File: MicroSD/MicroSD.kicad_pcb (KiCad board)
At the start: 2 copper layers, 25.4 x 26.7 mm, 18 parts, among them J1 Conn_01x04, J2 Conn_01x04, U1 AP7365, U2 4050

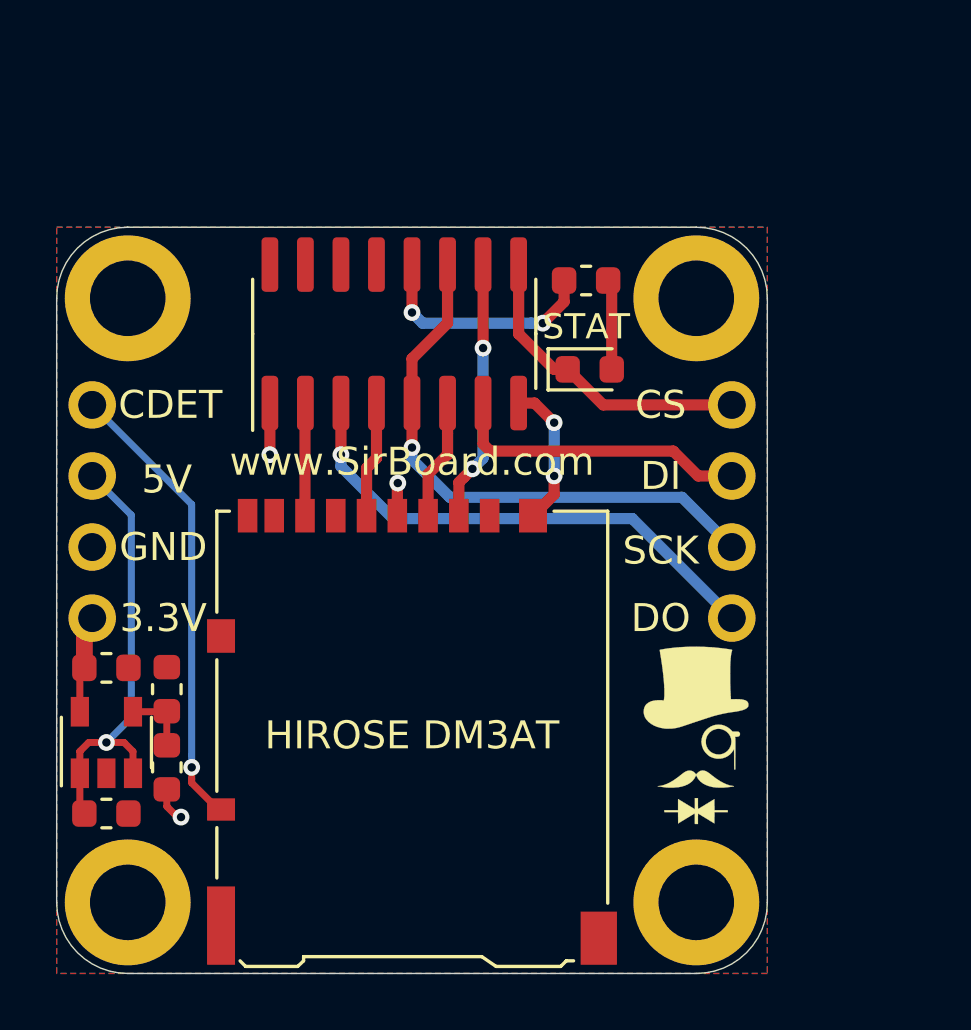
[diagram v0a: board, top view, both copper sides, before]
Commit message: MicroSDv2 Removed and MicroSD and MicroSD_DualVoltage Updated
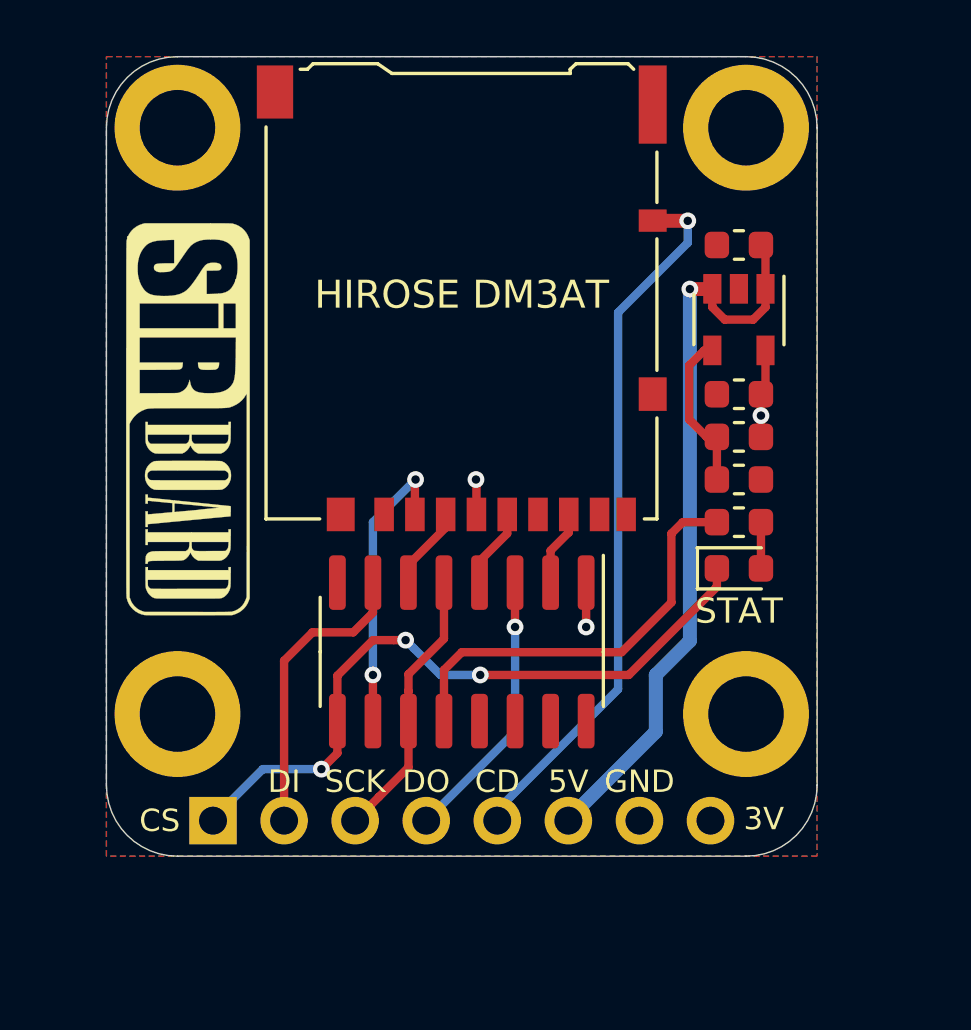
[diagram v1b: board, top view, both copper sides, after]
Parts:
- removed the G*** at (72.8, 43.1)
- removed J2: Conn_01x04, Connector_PinHeader_2.54mm:PinHeader_1x04_P2.54mm_Vertical
- added G***: LOGO, logo:SirBoard140x44, F.Cu at (54.6, 31.8)
- J1: value Conn_01x04 -> Conn_01x08; footprint Connector_PinHeader_2.54mm:PinHeader_1x04_P2.54mm_Vertical -> Connector_PinHeader_2.54mm:PinHeader_1x08_P2.54mm_Vertical; moved to B.Cu
- moved H3 35.4 mm to (74.5, 21.3), turned to 180 degrees
- moved H1 33.3 mm to (54.2, 21.3), turned to 180 degrees
- moved C1 30.4 mm to (74.3, 25.5), turned to 180 degrees
- moved U1 27.2 mm to (74.3, 28.2), turned to 270 degrees
- moved H4 26.6 mm to (74.5, 42.3), turned to 180 degrees
- moved C2 24.6 mm to (74.3, 30.9), turned to 180 degrees
- moved H2 23.8 mm to (54.2, 42.3), turned to 180 degrees
- moved J1 23.8 mm to (55.5, 46.1), turned to 270 degrees
- moved R1 23.6 mm to (74.3, 32.4), turned to 180 degrees
- moved R3 21.8 mm to (74.3, 33.9), turned to 0 degrees
- moved HIROSE DM3AT 15.6 mm to (64.4, 27.4), turned to 180 degrees
- moved U2 11.6 mm to (64.4, 40.1), turned to 270 degrees
- moved R6 10.2 mm to (74.3, 35.4)
- moved STAT 8.89 mm to (74.3, 37.1)
- moved G*** 6.59 mm to (64.4, 34.4)
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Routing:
- net CS: track 11.1 -> 24.8 mm, vias 0 -> 3
- net VIN: track 15.7 -> 26.8 mm
- net SCK: track 20.2 -> 9.82 mm, vias 1 -> 0
- net DETA: track 16.4 -> 25.5 mm
- net DO: track 18.5 -> 9.82 mm
- net Net-(R6-Pad1): track 8.38 -> 15.2 mm, vias 2 -> 0
- net GND: track 5.20 -> 0.00 mm, vias 2 -> 0
- net ADJ: track 2.44 -> 5.75 mm
- net VOUT: track 7.82 -> 6.00 mm
- net Net-(D1-Pad2): track 3.23 -> 1.65 mm
- net /CLK_SD: track 4.17 -> 2.85 mm
- net /DI_SD: track 4.31 -> 2.99 mm
- net /DO_SD: track 4.03 -> 2.71 mm
- net /CS_SD: track 9.33 -> 10.5 mm
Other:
- board size 25.4 x 26.7 mm -> 25.4 x 28.6 mm
- board text added: "3V"
- board text added: "CD"
- board text added: "MicroSD to DIP Breakout 74HC4050 Level-Shift"
- board text removed: "3.3V"
- board text removed: "5V to 3.3V Level Shift"
- board text removed: "CDET"
- board text removed: "MicroSD to DIP Breakout with"

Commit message: Board Redesign
Revision3
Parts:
- removed R1: 31K6, Resistor_SMD:R_0603_1608Metric
- removed R3: 10K, Resistor_SMD:R_0603_1608Metric
- added G***: LOGO, logo:logo42x59, F.Cu at (56.3, 26.3)
- C1, C2: value 1uF -> 10uF; footprint Capacitor_SMD:C_0603_1608Metric -> Capacitor_SMD:C_0805_2012Metric
- DM3AT: renamed from HIROSE DM3AT
- G***: footprint logo:logo126x178 -> logo:logo76x107
- G***: footprint logo:SirBoard140x44 -> logo:SirBoard112x35
- G***: footprint logo:SirBoard140x44 -> logo:SirBoard71X22
- H1, H2, H3, H4: footprint MountingHole:MountingHole_2.7mm_M2.5_ISO14580_Pad -> SirBoardLibrary:MountingHole_M2.5_SirBoard
- U1: value AP7365 -> AP2127K-3.3
- moved H2 23.8 mm to (78.0, 41.7), turned to 90 degrees
- moved H3 22.6 mm to (52.6, 26.4), turned to 90 degrees
- moved G*** 22.0 mm to (76.6, 30.6), turned to 0 degrees
- moved H1 20.4 mm to (52.6, 41.7), turned to 90 degrees
- moved H4 16.2 mm to (78.0, 26.4), turned to 90 degrees
- moved U2 12.0 mm to (54.1, 33.9), turned to 180 degrees
- moved C1 11.9 mm to (73.8, 37.5), turned to 90 degrees
- moved U1 9.56 mm to (76.6, 37.5), turned to 0 degrees
- moved C2 8.41 mm to (79.5, 37.5), turned to 270 degrees
- moved DM3AT 5.09 mm to (65.3, 32.4)
- moved STAT 4.90 mm to (78.5, 34.5), turned to 180 degrees
- moved J1 3.30 mm to (56.4, 42.9)
- moved G*** 2.57 mm to (65.3, 28.1)
- moved G*** 0.97 mm to (65.3, 34.0)
- moved R6 0.92 mm to (74.5, 34.5)
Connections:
- J1 pad 1: CS -> SCK
- J1 pad 3: SCK -> DO
- J1 pad 4: DO -> CS
- J1 pad 6: VIN -> VOUT
- J1 pad 8: VOUT -> VIN
- U1 pad 4: ADJ -> Net-(U1-Pad4)
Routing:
- net CS: track 24.8 -> 42.9 mm, vias 3 -> 1
- net VIN: track 26.8 -> 10.3 mm, vias 1 -> 0
- net /DI_SD: track 2.99 -> 19.1 mm
- net /CLK_SD: track 2.85 -> 17.7 mm
- net /CS_SD: track 10.5 -> 24.5 mm
- net SCK: track 9.82 -> 21.5 mm, vias 0 -> 1
- net /DO_SD: track 2.71 -> 14.3 mm
- net VOUT: track 6.00 -> 17.3 mm, vias 3 -> 1
- net GND: track 0.00 -> 10.6 mm, vias 0 -> 4
- net Net-(R6-Pad1): track 15.2 -> 22.6 mm, vias 0 -> 2
- net DETA: track 25.5 -> 18.6 mm
- net ADJ: track 5.75 -> 0.00 mm
- net DI: track 10.7 -> 15.1 mm, vias 0 -> 1
- net DO: track 9.82 -> 12.0 mm
- net Net-(D1-Pad2): track 1.65 -> 2.39 mm
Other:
- board size 25.4 x 28.6 mm -> 30.5 x 20.3 mm
- board text added: "MicroSD to DIP Breakout With 74HC4050 Level-Shift"
- board text removed: "MicroSD to DIP Breakout 74HC4050 Level-Shift"

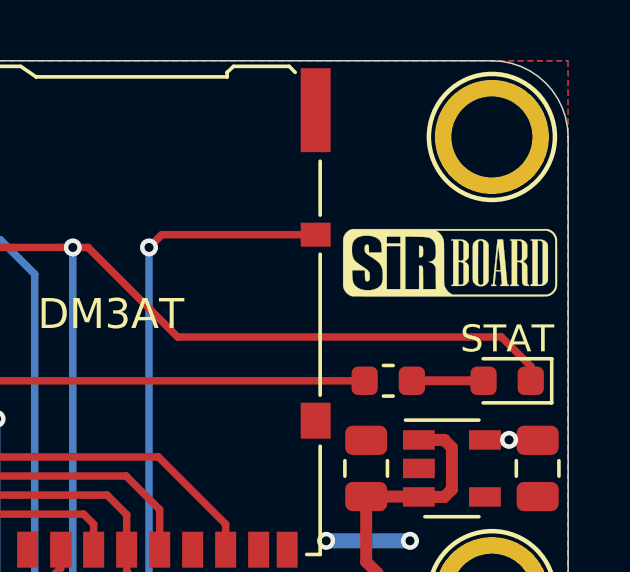
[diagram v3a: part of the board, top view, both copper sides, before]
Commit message: Breakout Boards Revision 2
Renders updated, silkscreen text improved, blurry silkscreen items removed/resized.
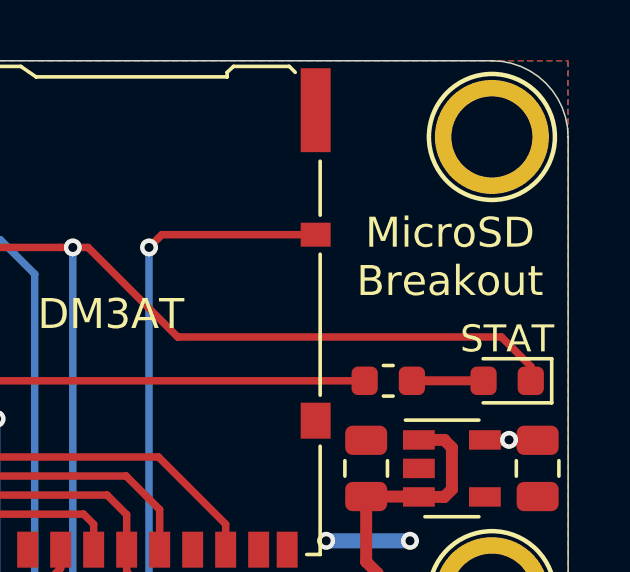
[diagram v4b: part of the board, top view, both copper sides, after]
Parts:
- removed the G*** at (76.6, 30.6)
- G***: footprint logo:SirBoard112x35 -> logo:SirBoard127x40
- moved G*** 0.25 mm to (65.3, 34.3)
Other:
- board text added: "MicroSD Breakout"
